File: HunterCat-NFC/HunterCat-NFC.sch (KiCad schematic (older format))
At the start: 27 parts

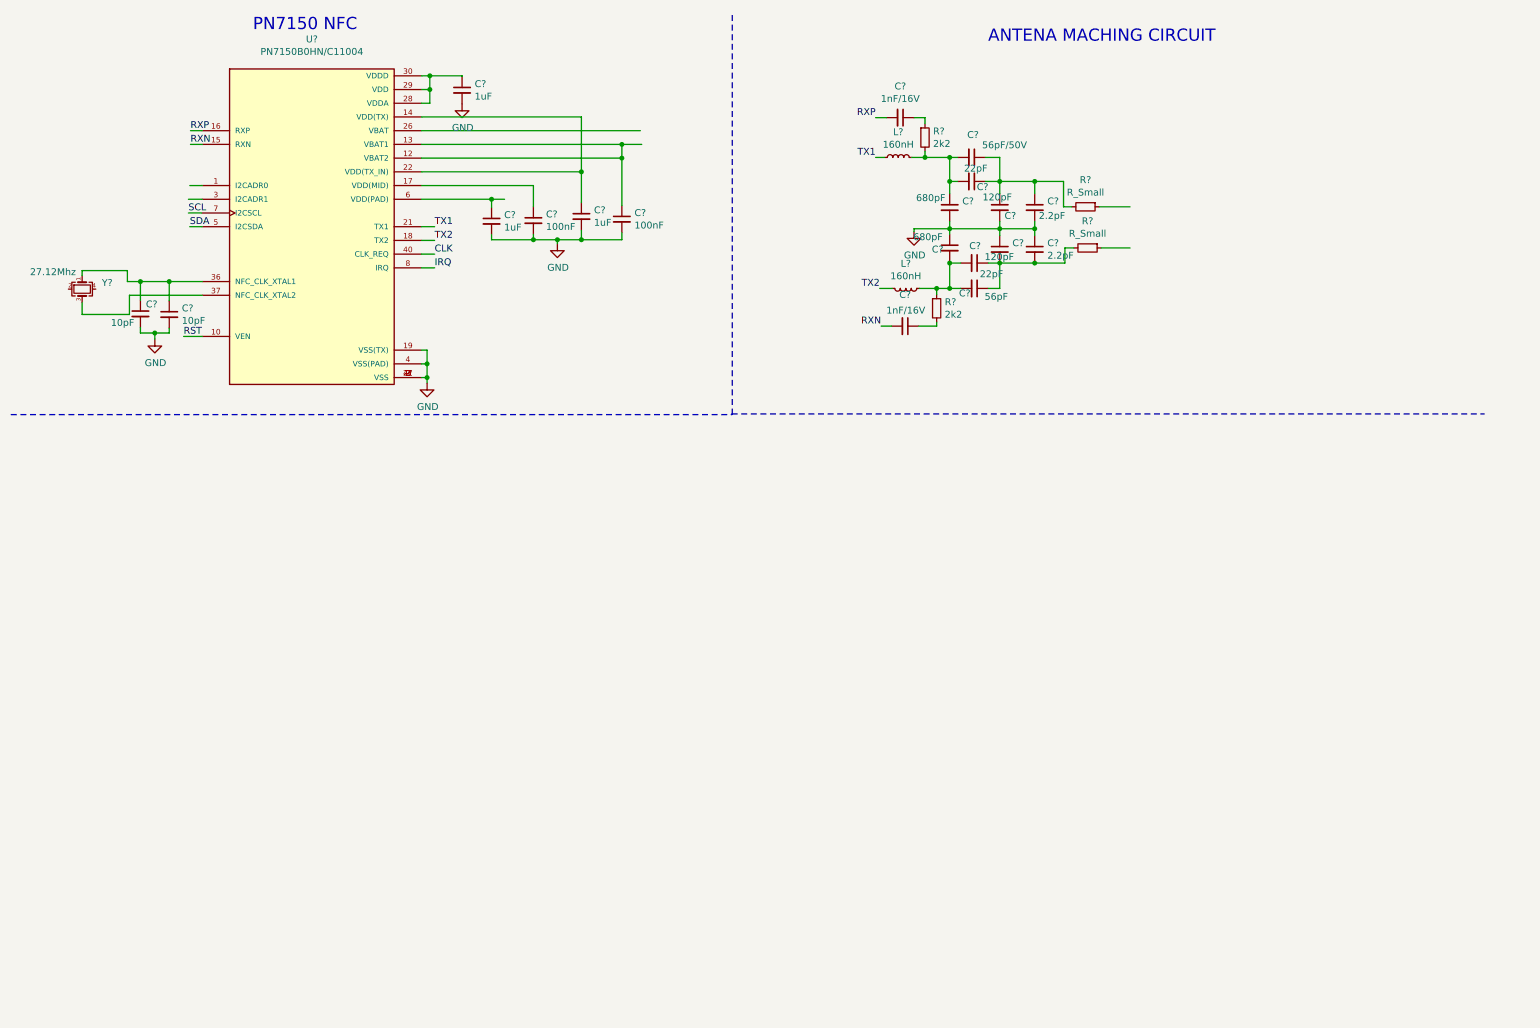
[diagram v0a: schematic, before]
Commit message: add samd21e
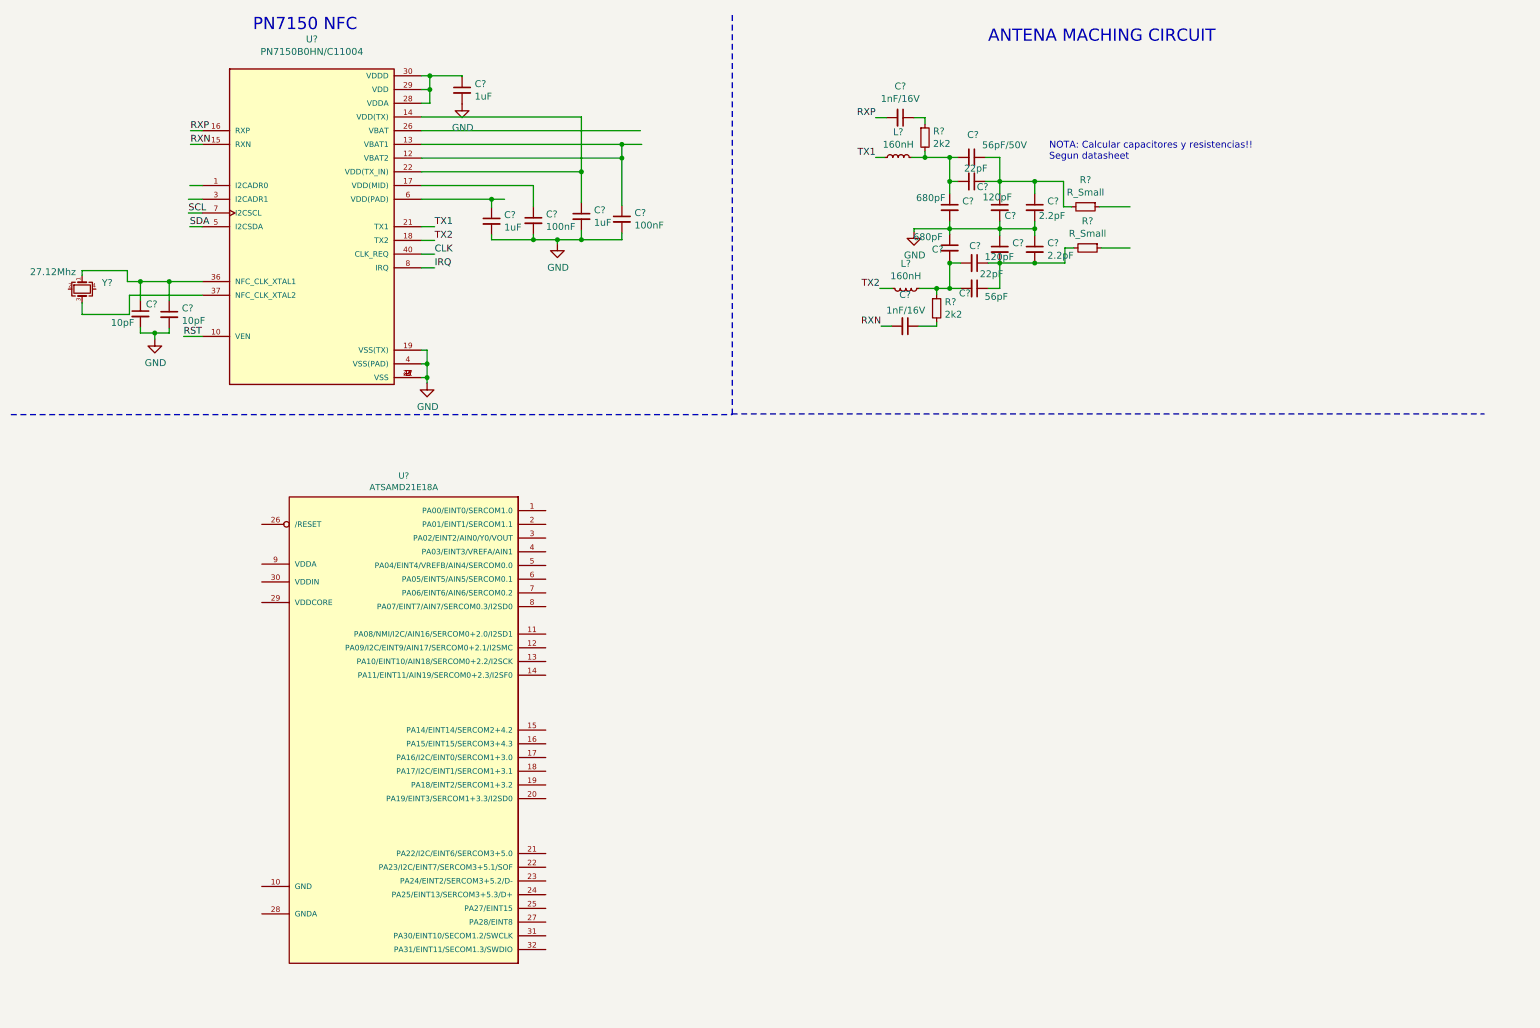
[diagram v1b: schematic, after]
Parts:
- added U?: ATSAMD21E18A, Package_QFP:TQFP-32_7x7mm_P0.8mm, symbol Electronic_Cats:ATSAMD21E18A
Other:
- note added: "NOTA: Calcular capacitores y resistencias!!\nSegun datasheet"
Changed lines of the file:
@@
 Wire Notes Line
 	5720 3405 11210 3405
+Text Notes 8035 1560 0    50   ~ 0
+NOTA: Calcular capacitores y resistencias!!\nSegun datasheet
+$Comp
+L Electronic_Cats:ATSAMD21E18A U?
+U 1 1 5E4D816D
+P 2965 5710
+F 0 "U?" H 3330 7564 45  0000 C CNN
+F 1 "ATSAMD21E18A" H 3330 7480 45  0000 C CNN
+F 2 "Package_QFP:TQFP-32_7x7mm_P0.8mm" H 2995 5860 20  0001 C CNN
+F 3 "https://www.mouser.mx/datasheet/2/268/SAM-D21-Family-Datasheet-DS40001882C-1381353.pdf" H 2965 5710 60  0001 C CNN
+	1    2965 5710
+	1    0    0    -1
+$EndComp
 $EndSCHEMATC

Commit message: alpha version
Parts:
- added C1: 0.1uF, symbol Device:C_Small
- added C16, C23, C24: 10uF, symbol Device:C_Small
- added C2: 1uF, symbol Device:C_Small
- added D1, D2, D? (x2): LED, symbol Device:LED
- added F1: 0.5A, symbol Device:Fuse_Small
- added J?: Battery, symbol Connector:Screw_Terminal_01x02
- added JP1, JP2: J_ADR0, symbol Jumper:SolderJumper_3_Bridged12
- added L3: L, symbol Device:L
- added P1: USB_C_Plug_USB2.0, symbol Connector:USB_C_Plug_USB2.0
- added R1, R16, R2: 10K, symbol Device:R_Small
- added R10, R12, R4, R? (x2): 1K, symbol Device:R_Small
- added R3, R5, R6, R7: 100K, symbol Device:R_Small
- added R8, R9: 5k1, symbol Device:R_Small
- added SW1: RESET, symbol Switch:SW_Push
- added U3: MCP73831-3-OT, Package_TO_SOT_SMD:SOT-23-5, symbol Battery_Management:MCP73831-3-OT
- added U4: AP2112K-3.3TRG1, SOT95P285X140-5N, symbol Electronic_Cats:AP2112K-3.3TRG1
- gave numbers to parts that had none: 28
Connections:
- net labels added: +3V3, +BATT, ADR0, ADR1, D+, D-, LED1, LED2, LED3, RESET, SWCLK, SWDIO, VBUS
- wire segments 115 -> 230
- no-connect marks 0 -> 12
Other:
- note added: "ANTENA"
- note added: "MICROCONTROLLER"
- note added: "NOTA: 5V??"
- note added: "REGULATOR AND BATTERY"
- moved on the sheet: U1

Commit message: add addres select I2C
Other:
- note added: "ADDRESS SELECT"
- moved on the sheet: C10, C11, C12, C13, C14, C15, C17, C18, C19, C20, C21, C22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

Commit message: update components
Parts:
- removed U4: AP2112K-3.3TRG1, SOT95P285X140-5N, symbol Electronic_Cats:AP2112K-3.3TRG1
- added U?: AP2112K-3.3, Package_TO_SOT_SMD:SOT-23-5, symbol Regulator_Linear:AP2112K-3.3
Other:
- moved on the sheet: C24
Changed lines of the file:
@@
 Text Notes 10280 1985 0    50   ~ 0
 ANTENA
-$Comp
-L Electronic_Cats:AP2112K-3.3TRG1 U4
-U 1 1 5E58A243
-P 10195 4340
-F 0 "U4" H 10195 4810 50  0000 C CNN
-F 1 "AP2112K-3.3TRG1" H 10195 4719 50  0000 C CNN
-F 2 "SOT95P285X140-5N" H 10195 4340 50  0001 L BNN
-F 3 "SOT-753 Diodes Inc." H 10195 4340 50  0001 L BNN
-F 4 "0.15 USD" H 10195 4340 50  0001 L BNN "Campo4"
-F 5 "Diodes Inc." H 10195 4340 50  0001 L BNN "Campo5"
-F 6 "AP2112K-3.3TRG1" H 10195 4340 50  0001 L BNN "Campo6"
-F 7 "Good" H 10195 4340 50  0001 L BNN "Campo7"
-F 8 "AP2112 Series 0.6 A 3.3 V Fixed Output SMT LDO Linear Regulator - SOT23-5" H 10195 4340 50  0001 L BNN "Campo8"
-	1    10195 4340
-	1    0    0    -1
-$EndComp
 Wire Wire Line
 	9695 4140 9525 4140
@@
 	9195 4140 9195 4090
 Wire Wire Line
-	10695 4140 10775 4140
-Wire Wire Line
-	10885 4140 10885 4085
-Wire Wire Line
-	10695 4540 10740 4540
-Wire Wire Line
-	10740 4540 10740 4665
+	10295 4140 10375 4140
+Wire Wire Line
+	10485 4140 10485 4085
+Wire Wire Line
+	9995 4540 9995 4665
 $Comp
 L power:GND #PWR031
 U 1 1 5E5A6C5C
-P 10740 4665
-F 0 "#PWR031" H 10740 4415 50  0001 C CNN
-F 1 "GND" H 10745 4492 50  0000 C CNN
-F 2 "" H 10740 4665 50  0001 C CNN
-F 3 "" H 10740 4665 50  0001 C CNN
-	1    10740 4665
+P 9995 4665
+F 0 "#PWR031" H 9995 4415 50  0001 C CNN
+F 1 "GND" H 10000 4492 50  0000 C CNN
+F 2 "" H 9995 4665 50  0001 C CNN
+F 3 "" H 9995 4665 50  0001 C CNN
+	1    9995 4665
 	1    0    0    -1
 $EndComp
@@
 L power:+3V3 #PWR033
 U 1 1 5E5A76AE
-P 10885 4085
-F 0 "#PWR033" H 10885 3935 50  0001 C CNN
-F 1 "+3V3" H 10900 4258 50  0000 C CNN
-F 2 "" H 10885 4085 50  0001 C CNN
-F 3 "" H 10885 4085 50  0001 C CNN
-	1    10885 4085
+P 10485 4085
+F 0 "#PWR033" H 10485 3935 50  0001 C CNN
+F 1 "+3V3" H 10500 4258 50  0000 C CNN
+F 2 "" H 10485 4085 50  0001 C CNN
+F 3 "" H 10485 4085 50  0001 C CNN
+	1    10485 4085
 	1    0    0    -1
 $EndComp
@@
 $EndComp
 Wire Wire Line
-	9695 4340 9610 4340
-Wire Wire Line
-	9610 4340 9610 4410
-Wire Wire Line
-	9610 4410 9525 4410
-Wire Wire Line
 	9525 4210 9525 4140
 Connection ~ 9525 4140
@@
 L Device:C_Small C24
 U 1 1 5E7362A4
-P 10775 4240
-F 0 "C24" H 10867 4286 50  0000 L CNN
-F 1 "10uF" H 10867 4195 50  0000 L CNN
-F 2 "" H 10775 4240 50  0001 C CNN
-F 3 "~" H 10775 4240 50  0001 C CNN
-	1    10775 4240
-	1    0    0    -1
-$EndComp
-Connection ~ 10775 4140
-Wire Wire Line
-	10775 4140 10885 4140
-Wire Wire Line
-	10775 4340 10775 4365
+P 10375 4240
+F 0 "C24" H 10467 4286 50  0000 L CNN
+F 1 "10uF" H 10467 4195 50  0000 L CNN
+F 2 "" H 10375 4240 50  0001 C CNN
+F 3 "~" H 10375 4240 50  0001 C CNN
+	1    10375 4240
+	1    0    0    -1
+$EndComp
+Connection ~ 10375 4140
+Wire Wire Line
+	10375 4140 10485 4140
+Wire Wire Line
+	10375 4340 10375 4365
 Wire Wire Line
 	9325 4340 9325 4380
@@
 L power:GND #PWR032
 U 1 1 5E751149
-P 10775 4365
-F 0 "#PWR032" H 10775 4115 50  0001 C CNN
-F 1 "GND" H 10835 4235 50  0000 C CNN
-F 2 "" H 10775 4365 50  0001 C CNN
-F 3 "" H 10775 4365 50  0001 C CNN
-	1    10775 4365
+P 10375 4365
+F 0 "#PWR032" H 10375 4115 50  0001 C CNN
+F 1 "GND" H 10435 4235 50  0000 C CNN
+F 2 "" H 10375 4365 50  0001 C CNN
+F 3 "" H 10375 4365 50  0001 C CNN
+	1    10375 4365
 	1    0    0    -1
 $EndComp
@@
 Wire Notes Line
 	7850 470  7840 470
+$Comp
+L Regulator_Linear:AP2112K-3.3 U?
+U 1 1 5E451F7B
+P 9995 4240
+F 0 "U?" H 9995 4582 50  0000 C CNN
+F 1 "AP2112K-3.3" H 9995 4491 50  0000 C CNN
+F 2 "Package_TO_SOT_SMD:SOT-23-5" H 9995 4565 50  0001 C CNN
+F 3 "https://www.diodes.com/assets/Datasheets/AP2112.pdf" H 9995 4340 50  0001 C CNN
+	1    9995 4240
+	1    0    0    -1
+$EndComp
+Wire Wire Line
+	9695 4240 9595 4240
+Wire Wire Line
+	9595 4240 9595 4440
+Wire Wire Line
+	9595 4440 9525 4440
+Wire Wire Line
+	9525 4440 9525 4410
 $EndSCHEMATC
